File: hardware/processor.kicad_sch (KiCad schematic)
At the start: 6 parts, among them SW1 RESET, SW2 BOOT, U6 ESP32-S3-WROOM-1

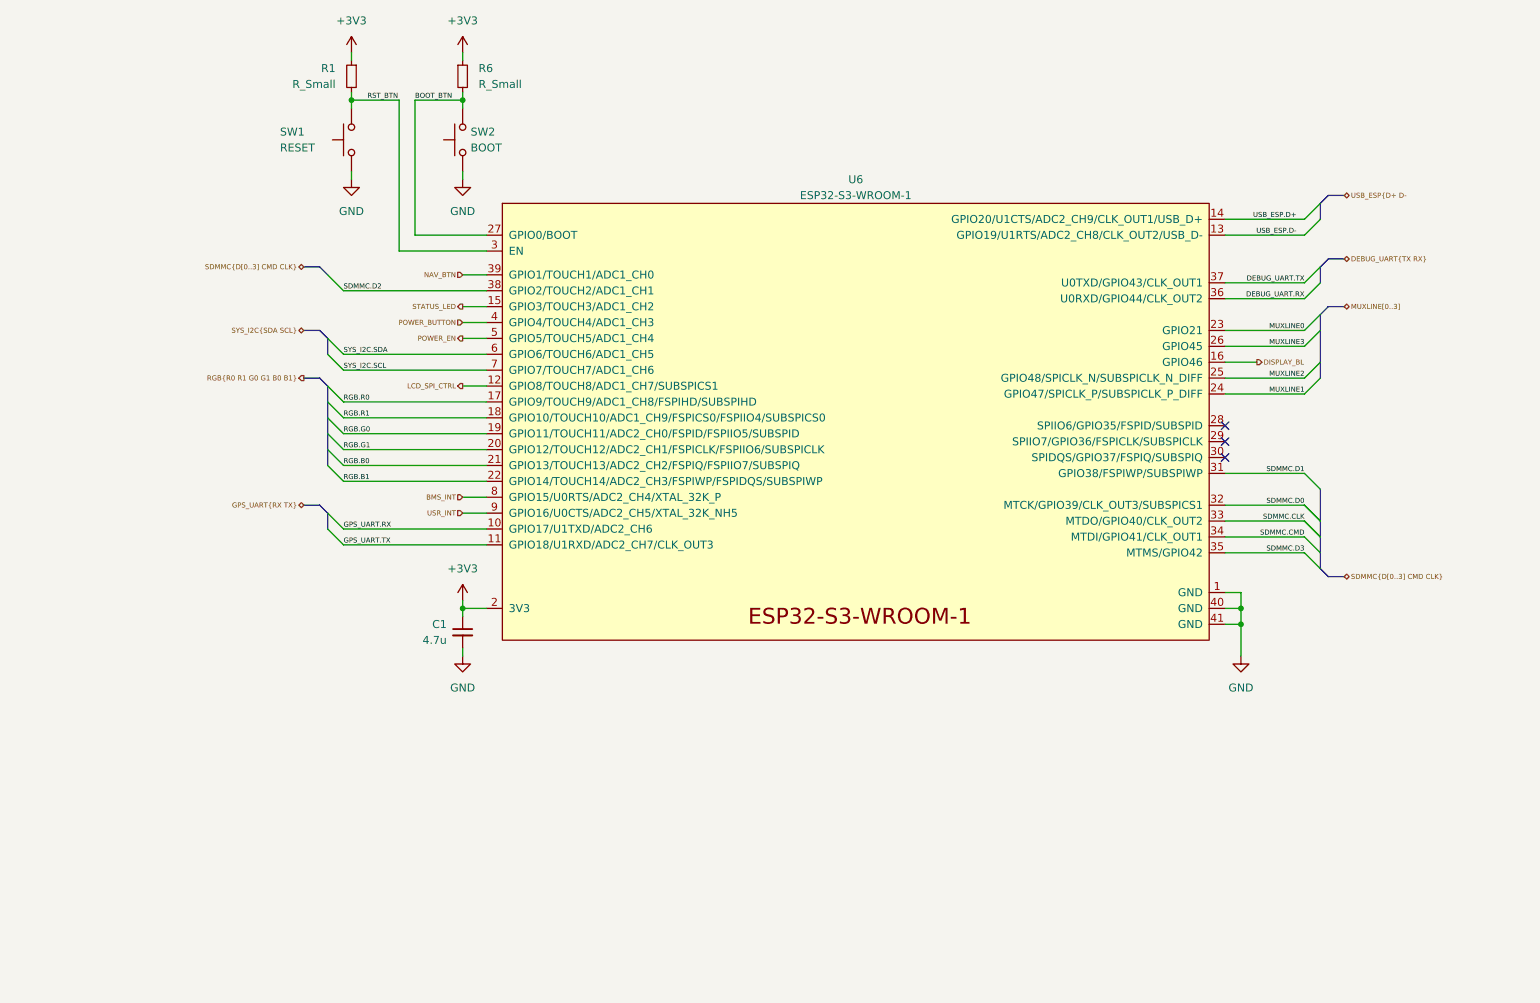
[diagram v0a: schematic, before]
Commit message: merged in lcdboard test work
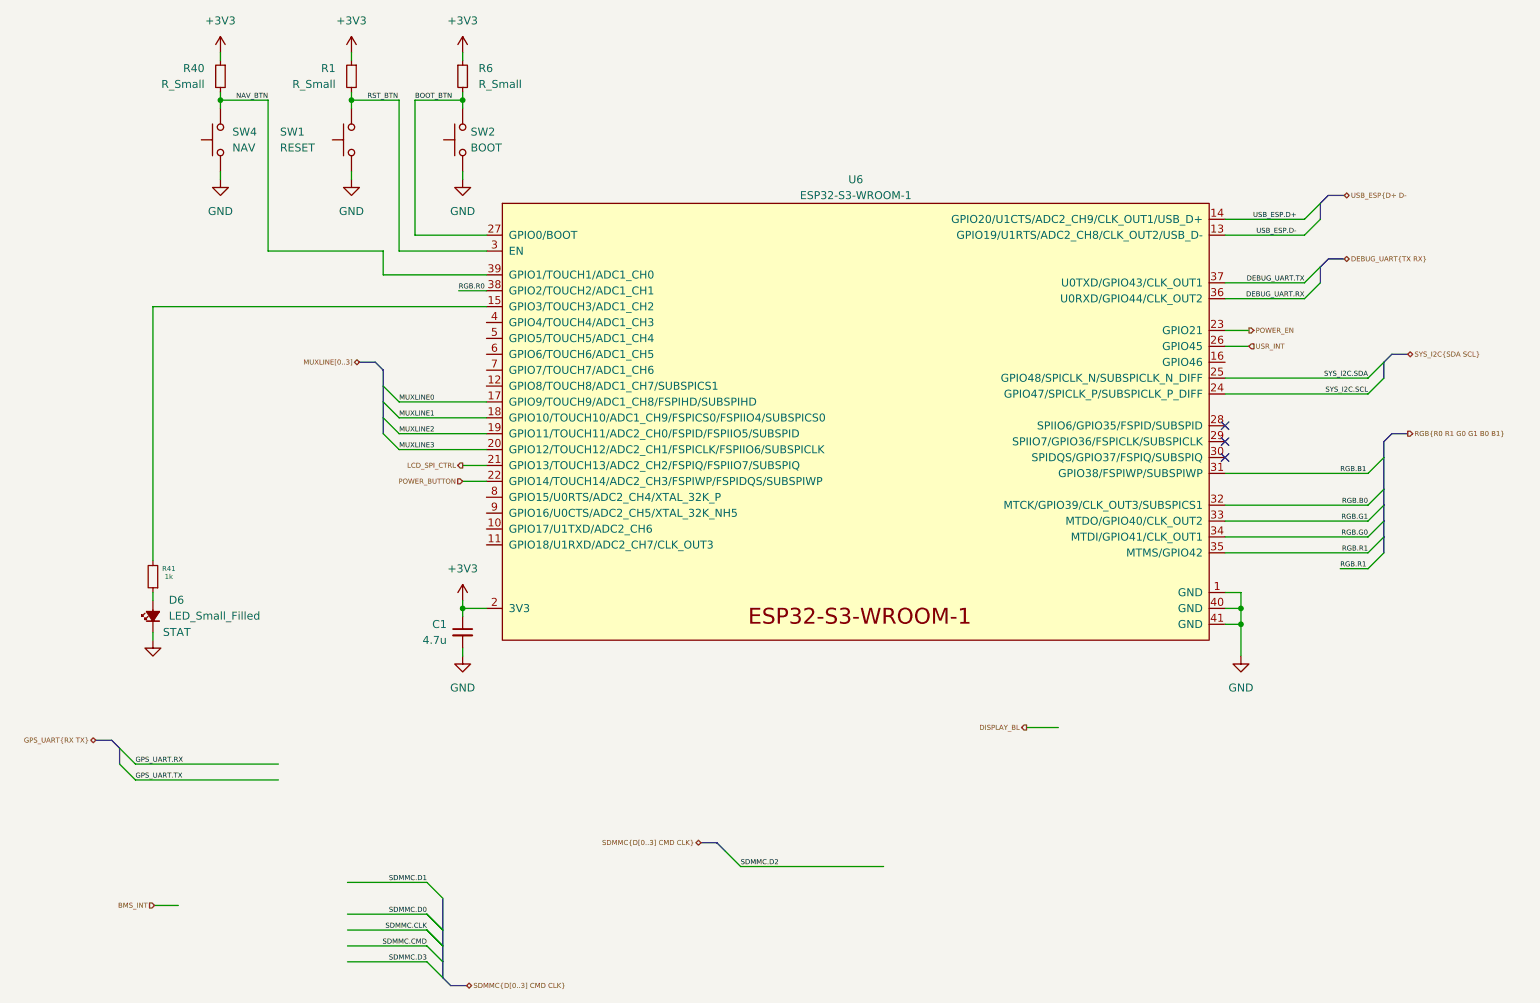
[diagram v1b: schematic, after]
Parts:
- added D6: LED_Small_Filled, LED_SMD:LED_0402_1005Metric, symbol Device:LED_Small_Filled
- added R40: R_Small, Resistor_SMD:R_0402_1005Metric, symbol Device:R_Small
- added R41: 1k, Resistor_SMD:R_0402_1005Metric, symbol Device:R_Small
- added SW4: NAV, Button_Switch_SMD:SW_SPST_B3U-1000P, symbol Switch:SW_Push
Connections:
- net +3V3: now also R40.1
- net BMS_INT: no longer U6.8 (GPIO15/U0RTS/ADC2_CH4/XTAL_32K_P)
- net DISPLAY_BL: no longer U6.16 (GPIO46)
- net GND: now also D6.1 (K), SW4.1
- net GPS_UART.RX: no longer U6.10 (GPIO17/U1TXD/ADC2_CH6)
- net GPS_UART.TX: no longer U6.11 (GPIO18/U1RXD/ADC2_CH7/CLK_OUT3)
- net LCD_SPI_CTRL: now also U6.21 (GPIO13/TOUCH13/ADC2_CH2/FSPIQ/FSPIIO7/SUBSPIQ); no longer U6.12 (GPIO8/TOUCH8/ADC1_CH7/SUBSPICS1)
- net MUXLINE0: now also U6.17 (GPIO9/TOUCH9/ADC1_CH8/FSPIHD/SUBSPIHD); no longer U6.23 (GPIO21)
- net MUXLINE1: now also U6.18 (GPIO10/TOUCH10/ADC1_CH9/FSPICS0/FSPIIO4/SUBSPICS0); no longer U6.24 (GPIO47/SPICLK_P/SUBSPICLK_P_DIFF)
- net MUXLINE2: now also U6.19 (GPIO11/TOUCH11/ADC2_CH0/FSPID/FSPIIO5/SUBSPID); no longer U6.25 (GPIO48/SPICLK_N/SUBSPICLK_N_DIFF)
- net MUXLINE3: now also U6.20 (GPIO12/TOUCH12/ADC2_CH1/FSPICLK/FSPIIO6/SUBSPICLK); no longer U6.26 (GPIO45)
- net NAV_BTN: now also R40.2, SW4.2
- net POWER_BUTTON: now also U6.22 (GPIO14/TOUCH14/ADC2_CH3/FSPIWP/FSPIDQS/SUBSPIWP); no longer U6.4 (GPIO4/TOUCH4/ADC1_CH3)
- net POWER_EN: now also U6.23 (GPIO21); no longer U6.5 (GPIO5/TOUCH5/ADC1_CH4)
- net RGB.B0: now also U6.32 (MTCK/GPIO39/CLK_OUT3/SUBSPICS1); no longer U6.21 (GPIO13/TOUCH13/ADC2_CH2/FSPIQ/FSPIIO7/SUBSPIQ)
- net RGB.B1: now also U6.31 (GPIO38/FSPIWP/SUBSPIWP); no longer U6.22 (GPIO14/TOUCH14/ADC2_CH3/FSPIWP/FSPIDQS/SUBSPIWP)
- net RGB.G0: now also U6.34 (MTDI/GPIO41/CLK_OUT1); no longer U6.19 (GPIO11/TOUCH11/ADC2_CH0/FSPID/FSPIIO5/SUBSPID)
- net RGB.G1: now also U6.33 (MTDO/GPIO40/CLK_OUT2); no longer U6.20 (GPIO12/TOUCH12/ADC2_CH1/FSPICLK/FSPIIO6/SUBSPICLK)
- net RGB.R0: now also U6.38 (GPIO2/TOUCH2/ADC1_CH1); no longer U6.17 (GPIO9/TOUCH9/ADC1_CH8/FSPIHD/SUBSPIHD)
- net RGB.R1: now also U6.35 (MTMS/GPIO42); no longer U6.18 (GPIO10/TOUCH10/ADC1_CH9/FSPICS0/FSPIIO4/SUBSPICS0)
- net SDMMC.CLK: no longer U6.33 (MTDO/GPIO40/CLK_OUT2)
- net SDMMC.CMD: no longer U6.34 (MTDI/GPIO41/CLK_OUT1)
- net SDMMC.D0: no longer U6.32 (MTCK/GPIO39/CLK_OUT3/SUBSPICS1)
- net SDMMC.D1: no longer U6.31 (GPIO38/FSPIWP/SUBSPIWP)
- net SDMMC.D2: no longer U6.38 (GPIO2/TOUCH2/ADC1_CH1)
- net SDMMC.D3: no longer U6.35 (MTMS/GPIO42)
- net SYS_I2C.SCL: now also U6.24 (GPIO47/SPICLK_P/SUBSPICLK_P_DIFF); no longer U6.7 (GPIO7/TOUCH7/ADC1_CH6)
- net SYS_I2C.SDA: now also U6.25 (GPIO48/SPICLK_N/SUBSPICLK_N_DIFF); no longer U6.6 (GPIO6/TOUCH6/ADC1_CH5)
- net USR_INT: now also U6.26 (GPIO45); no longer U6.9 (GPIO16/U0CTS/ADC2_CH5/XTAL_32K_NH5)
- net STATUS_LED: no longer names the net of U6.15 (GPIO3/TOUCH3/ADC1_CH2)
- net STATUS_LED: now also R41.2
- new net: D6.2 (A), R41.1
